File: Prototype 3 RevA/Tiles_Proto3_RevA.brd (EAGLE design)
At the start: 160 x 100 mm, 34 parts, among them IC1 LSM9DS1, SW1 MF-SW-TACT-4.2MM, U1 RFD77101

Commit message: routing finshed
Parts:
- removed BAT+, BAT-: (no value), wirepad:SMD1,27-2,54
- removed H1, H2, H3, H4: MOUNT-PAD-ROUND2.8, holes:2,8-PAD
- removed IC1: LSM9DS1, LSM9DS1:LGA24_3.5X3.1MM
- removed J2, J3: (no value), SparkFun-Connectors:1X04_NO_SILK
- removed J4: (no value), tiles:1X04_NO_SILK
- removed J5: (no value), tiles:1X04_NO_SILK_RND
- removed SW1: MF-SW-TACT-4.2MM, MF_Switches:TACT4.2MM
- removed U$21: 9MBUZ, tiles:BUZPKG
- added B+, B-: (no value), wirepad:1,6/0,8
- added BATT1: BAT-HLD-001, tiles:BAT-HLD-001
- added BT1: (no value), SparkFun-Batteries:BATTCON_12MM
- added BT2: (no value), SparkFun-Batteries:BATTCON_20MM
- added CAP: (no value), SparkFun-Connectors:1X02_NO_SILK
- added CAP-A, CAP-B, IO-2, IO-3: MOUNT-PAD-ROUND2.5, tiles:2,5-PAD-SIM
- added D2: MF-LED-0603-RED, MF_LEDs:LED0603
- added GROVE-GPIO: (no value), SparkFun-Connectors:1X04_NO_SILK
- added GROVE-I2C: (no value), tiles:1X04_NO_SILK_LNG
- added HAPTIC: DRV2605L, SparkFun-IC-Special-Function:VSSOP-10
- added IMU: LSM9DS1, LSM9DS1:LGA24_3.5X3.1MM
- added JP1: JUMPER-SMT_2_NO_NO-SILK, SparkFun-Jumpers:SMT-JUMPER_2_NO_NO-SILK
- added R6: 330, MF_Passives:R0603
- added R7: 10K 1/10W, Seeed-OPL-Resistor:R0603
- added R8: 1K 1/10W, Seeed-OPL-Resistor:R0603
- added SW2: MF-SW-TACT-4.2MM, MF_Switches:TACT4.2MM
- added TOUCH: (no value), cap1188-microbuilder:QFN24_4MM_SMSC
- C1: value 10uf -> 1uf
- J1: device SparkFun-Connectors:1X07 -> tiles:1X07_NO_SILK_SQUAREPADS
- M+, M-: device wirepad:SMD1,27-2,54 -> wirepad:1,6/0,8
- U$1: value DRV2605L -> 4MBUZ; device SparkFun-IC-Special-Function:VSSOP-10 -> tiles:BUZPKG
- U2: value (none) -> MF-DSC-SOT233-MMBT3904; device cap1188-microbuilder:QFN24_4MM_SMSC -> MF_Discrete_Semiconductor:SOT-23-3
- moved U2 25.1 mm to (87.8, 59.8), turned to 180 degrees
- moved D1 17.3 mm to (72.8, 70.7), turned to 180 degrees
- moved U$1 14.7 mm to (94.4, 59.3)
- moved R3 12.7 mm to (72.6, 60.7), turned to 90 degrees
- moved R4 11.2 mm to (71.8, 66.9), turned to 90 degrees
- moved C5 10.4 mm to (68.1, 66.8)
- moved C1 10.3 mm to (67.9, 70.7), turned to 270 degrees
- moved R5 6.68 mm to (72.7, 62.8), turned to 270 degrees
- moved J1 6.46 mm to (72.4, 86.0)
- moved C8 6.32 mm to (80.0, 63.7)
- moved C7 6.22 mm to (92.3, 73.1)
- moved LED1 6.13 mm to (80.0, 67.6)
- moved M- 5.61 mm to (69.5, 82.7)
- moved M+ 5.50 mm to (73.6, 82.7)
- moved U1 5.16 mm to (67.2, 73.7)
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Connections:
- removed net CAPINT: R3.1, U1.41, U2.13
- removed net CAPRES: R4.2, U1.40, U2.24
- removed net GPIO16: J1.7, U1.14
- new net +: BT1.PWR@1, BT2.1
- new net -: BT1.GND, BT2.2
- new net BTN: SW2.P$3, U1.14
- new net CAP-A: CAP-A.B2,8, CAP.1, TOUCH.22
- new net CAP-B: CAP-B.B2,8, CAP.2, TOUCH.21
- new net CAP-INT: R3.1, TOUCH.13, U1.15
- new net CAP-RES: R4.2, TOUCH.24, U1.16
- new net IMU-INT: IMU.11, U1.20
- new net IO-2: GROVE-GPIO.1, IO-2.B2,8, J1.7, U1.24
- new net IO-3: GROVE-GPIO.2, IO-3.B2,8, U1.22
- new net N$10: IMU.10
- new net N$12: IMU.12
- new net N$9: D2.ANODE, R6.P$2
- net BUZZER: now also R7.2, U1.26, U2.P$1; no longer U$21.P$1, U1.13
- net GND: now also B-.1, BATT1.NEG_0, C5.2, C7.1, D2.CATHODE, GROVE-GPIO.4, GROVE-I2C.1, HAPTIC.P$8, IMU.14, IMU.15, IMU.16, IMU.17, IMU.18, IMU.19, IMU.20, R7.1, SW2.P$1, TOUCH.1, TOUCH.THERM, U2.P$2; no longer BAT-.1, IC1.14, IC1.15, IC1.16, IC1.17, IC1.18, IC1.19, IC1.20, SW1.P$1, U$1.P$8, U$21.P$2, U2.THERM
- net N$1: now also IMU.21; no longer IC1.21
- net N$2: now also IMU.24; no longer IC1.24
- net N$3: now also TOUCH.14; no longer U2.14
- net N$4: now also R8.1, U$1.BZ-, U2.P$3; no longer C5.2, U2.23
- net N$5: now also HAPTIC.P$1; no longer U$1.P$1
- net N$6: now also J1.4, JP1.2; no longer C7.1, U$1.P$10, U$1.P$5, U$1.P$6
- net N$7: now also HAPTIC.P$9; no longer U$1.P$9
- net N$8: now also HAPTIC.P$7; no longer U$1.P$7
- net NEOPIX: now also U1.18; no longer U1.11
- net PWRBTN: no longer SW1.P$3
- net SCL: now also GROVE-I2C.4, HAPTIC.P$2, IMU.2, TOUCH.4; no longer IC1.2, U$1.P$2, U2.4
- net SDA: now also GROVE-I2C.3, HAPTIC.P$3, IMU.4, TOUCH.3; no longer IC1.4, U$1.P$3, U2.3
- net STATLED: now also R6.P$1
- net VCC: now also GROVE-GPIO.3, GROVE-I2C.2, HAPTIC.P$10, HAPTIC.P$5, HAPTIC.P$6, IMU.1, IMU.13, IMU.22, IMU.23, IMU.3, IMU.7, IMU.8, R8.2, TOUCH.23, U$1.BZ+; no longer IC1.1, IC1.13, IC1.22, IC1.23, IC1.3, IC1.7, IC1.8
- net V_BATT: now also B+.1, BATT1.POS_0, BATT1.POS_1, JP1.1; no longer BAT+.1, J1.4
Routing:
- net GND: track 0.00 -> 173.0 mm, vias 0 -> 20
- net VCC: track 0.00 -> 167.1 mm, vias 0 -> 6
- net V_BATT: track 0.00 -> 110.9 mm, vias 0 -> 3
- net SDA: track 0.00 -> 77.7 mm, vias 0 -> 3
- net SCL: track 0.00 -> 74.1 mm, vias 0 -> 6
- net IO-3: track 0.00 -> 55.9 mm, vias 0 -> 2
- net BUZZER: track 0.00 -> 44.1 mm, vias 0 -> 2
- net N$8: track 0.00 -> 43.4 mm, vias 0 -> 1
- net IO-2: track 0.00 -> 40.4 mm, vias 0 -> 1
- net N$7: track 0.00 -> 34.5 mm, vias 0 -> 2
- net IMU-INT: track 0.00 -> 27.3 mm, vias 0 -> 2
- net CAP-A: track 0.00 -> 26.5 mm, vias 0 -> 1
- net CAP-B: track 0.00 -> 24.0 mm, vias 0 -> 1
- net CAP-INT: track 0.00 -> 21.4 mm, vias 0 -> 2
- net CAP-RES: track 0.00 -> 21.3 mm, vias 0 -> 2
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
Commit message: finished cleanup
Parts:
- removed BT1: (no value), SparkFun-Batteries:BATTCON_12MM
- removed BT2: (no value), SparkFun-Batteries:BATTCON_20MM
- moved GROVE-I2C 0.81 mm to (76.2, 54.7)
- moved LED1 0.56 mm to (80.0, 67.1)
- moved C8 0.20 mm to (80.0, 63.5)
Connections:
- removed net +: BT1.PWR@1, BT2.1
- removed net -: BT1.GND, BT2.2
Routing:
- net VCC: track 167.1 -> 165.4 mm
- net SDA: track 77.7 -> 76.2 mm
- net GND: track 173.0 -> 174.4 mm
- net SCL: track 74.1 -> 73.5 mm

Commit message: added text
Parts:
- CAP: device SparkFun-Connectors:1X02_NO_SILK -> cap1188-microbuilder:QFN24_4MM_SMSC
- TOUCH: device cap1188-microbuilder:QFN24_4MM_SMSC -> SparkFun-Connectors:1X02_NO_SILK
- moved CAP 10.7 mm to (66.6, 60.6), turned to 0 degrees
- moved TOUCH 10.7 mm to (64.0, 71.1), turned to 270 degrees
- moved C8 0.22 mm to (79.9, 63.3)
- renumbered D2 to STAT, GROVE-GPIO to GPIO, GROVE-I2C to I2C, LED1 to LED, SW2 to SW, U$1 to BUZZER, U1 to SIMBLEE
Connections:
- net CAP-A: now also CAP.22, TOUCH.1; no longer CAP.1, TOUCH.22
- net CAP-B: now also CAP.21, TOUCH.2; no longer CAP.2, TOUCH.21
- net CAP-INT: now also CAP.13; no longer TOUCH.13
- net CAP-RES: now also CAP.24; no longer TOUCH.24
- net GND: now also CAP.1, CAP.THERM; no longer TOUCH.1, TOUCH.THERM
- net N$3: now also CAP.14; no longer TOUCH.14
- net SCL: now also CAP.4; no longer TOUCH.4
- net SDA: now also CAP.3; no longer TOUCH.3
- net VCC: now also CAP.23; no longer TOUCH.23
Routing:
- net BUZZER: track 43.9 -> 44.6 mm
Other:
- board text added: "BAT"
- board text added: "GND"
- board text added: "HAPTIC"
- board text added: "IO-2"
- board text added: "IO-3"
- board text added: "IO2"
- board text added: "IO3"
- board text added: "MOTOR"
- board text added: "P#3 RevA (2017)"
- board text added: "RST"
- board text added: "RX"
- board text added: "SCL"
- board text added: "SDA"
- board text added: "Simone Mora"
- board text added: "T-A"
- board text added: "T-B"
- board text added: "TX"
- board text added: "VCC"
- board text added: "tilestoolkit.io"

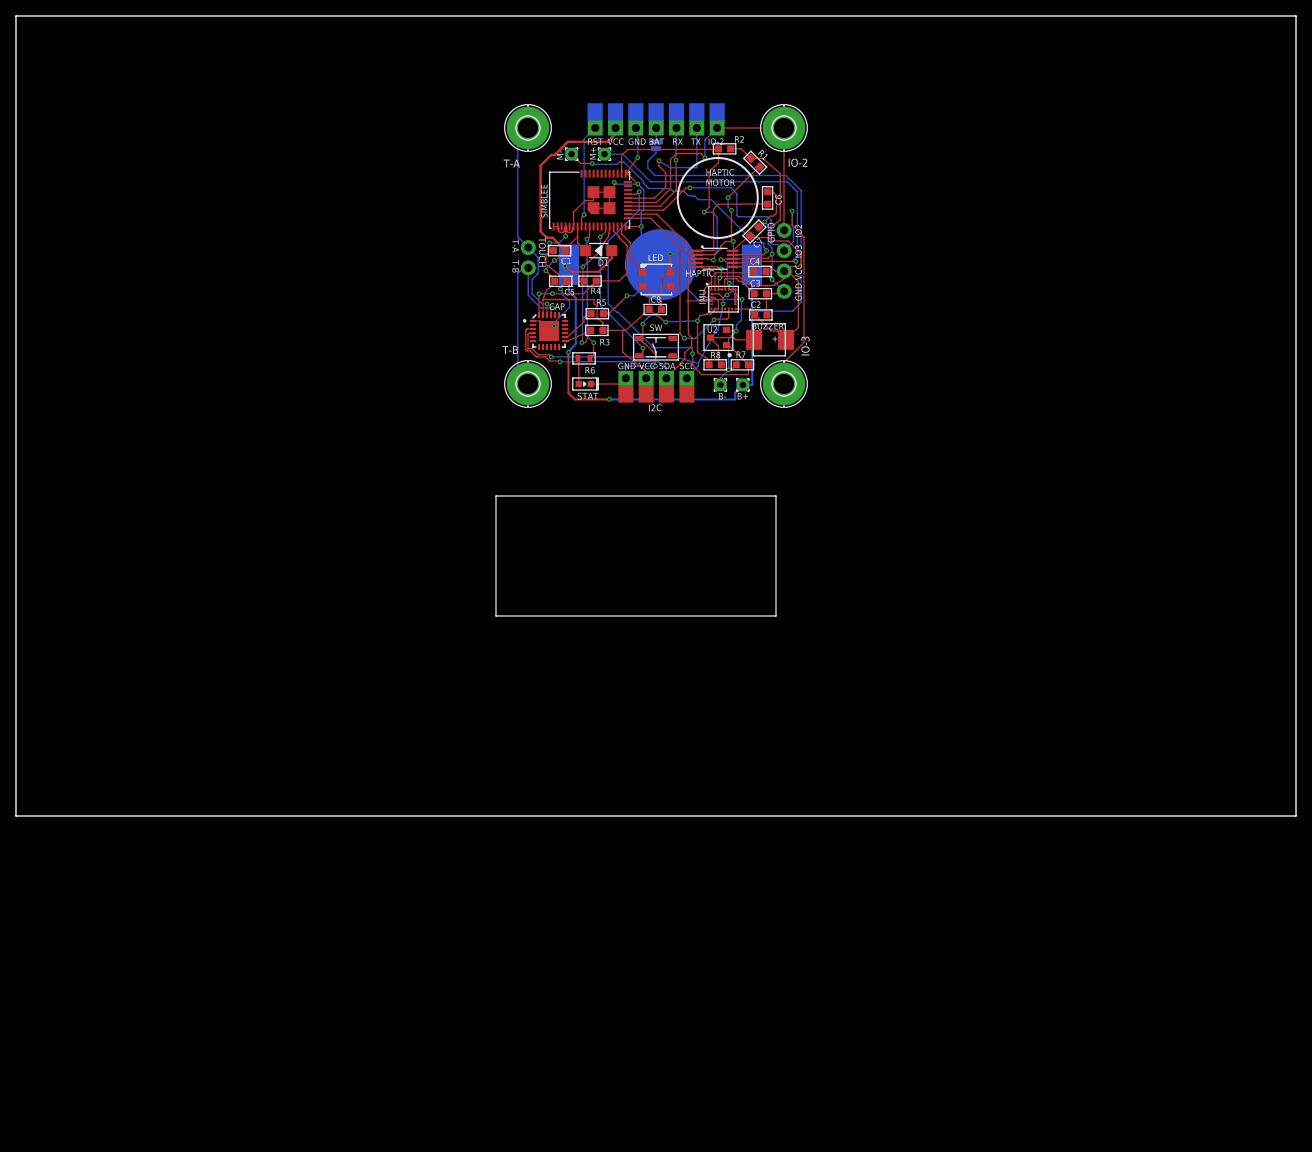
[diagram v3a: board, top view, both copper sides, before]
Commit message: finished silkscreen
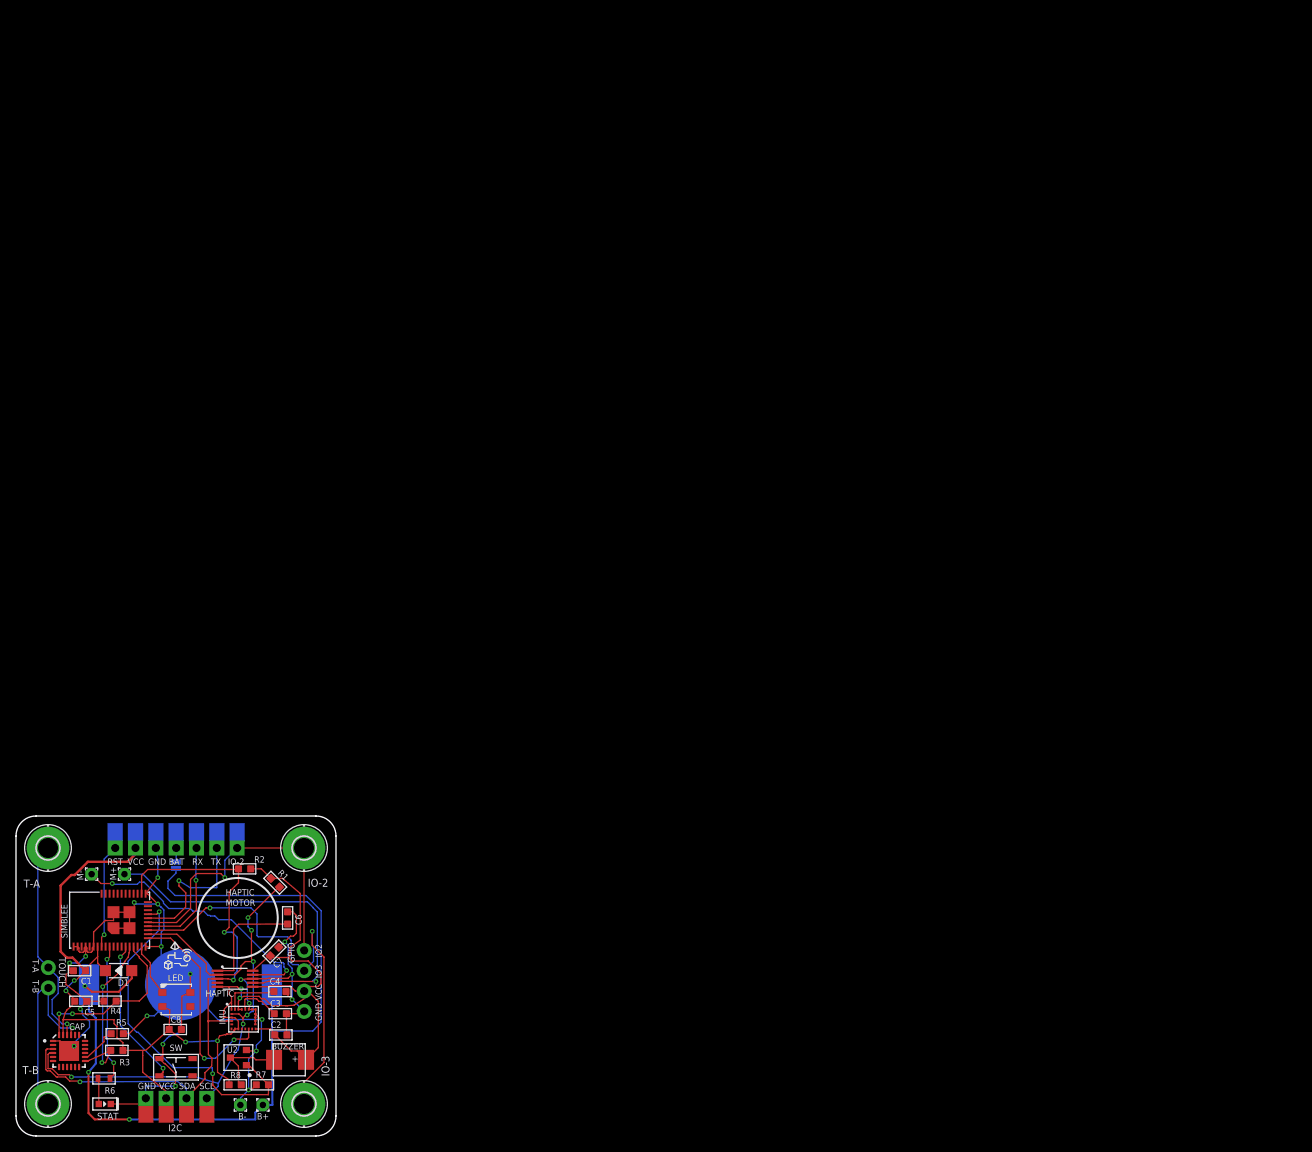
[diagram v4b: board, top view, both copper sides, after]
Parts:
- removed JP1: JUMPER-SMT_2_NO_NO-SILK, SparkFun-Jumpers:SMT-JUMPER_2_NO_NO-SILK
- added BATT_CHG: JUMPER-SMT_2_NO_NO-SILK, SparkFun-Jumpers:SMT-JUMPER_2_NO_NO-SILK
- moved B+ 108.2 mm to (30.9, -36.1)
- moved B- 108.2 mm to (28.1, -36.1)
- moved BATT1 108.2 mm to (20.6, -21.1)
- moved BUZZER 108.2 mm to (34.4, -30.7)
- moved C1 108.2 mm to (7.94, -19.3)
- moved C2 108.2 mm to (33.1, -27.4)
- moved C3 108.2 mm to (33.0, -24.7)
- moved C4 108.2 mm to (33.0, -21.9)
- moved C5 108.2 mm to (8.10, -23.2)
- moved C6 108.2 mm to (34.0, -12.7)
- moved C7 108.2 mm to (32.3, -16.9)
- moved C8 108.2 mm to (19.9, -26.7)
- moved CAP 108.2 mm to (6.63, -29.4)
- moved CAP-A 108.2 mm to (4.00, -4.00)
- moved CAP-B 108.2 mm to (4.00, -36.0)
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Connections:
- net N$6: now also BATT_CHG.2; no longer JP1.2
- net V_BATT: now also BATT_CHG.1; no longer JP1.1
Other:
- board size 160 x 100 mm -> 40 x 40 mm
- board text added: "/Users/Simone/Desktop/noun_143916_cc.bmp"
